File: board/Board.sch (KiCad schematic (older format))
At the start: 57 parts, among them J1 CONN_02X10, J10 CONN_01X03, J11 CONN_01X03, J12 CONN_01X02, J15 GS3, J16 GS3, J17 GS3, J18 GS2, J19 CONN_01X01, J2 CONN_01X03, J3 CONN_01X03, J4 CONN_01X03, J5 CONN_01X03, J6 CONN_01X03, J7 CONN_01X03, J8 CONN_01X03, J9 CONN_01X03, SW1 SW_Push, U1 STM32F410RBTx, U2 LF33ABDT-TR, U3 ICM-20689, U4 SN74LVC1G04, U5 MS5611, Y1 25 MHz

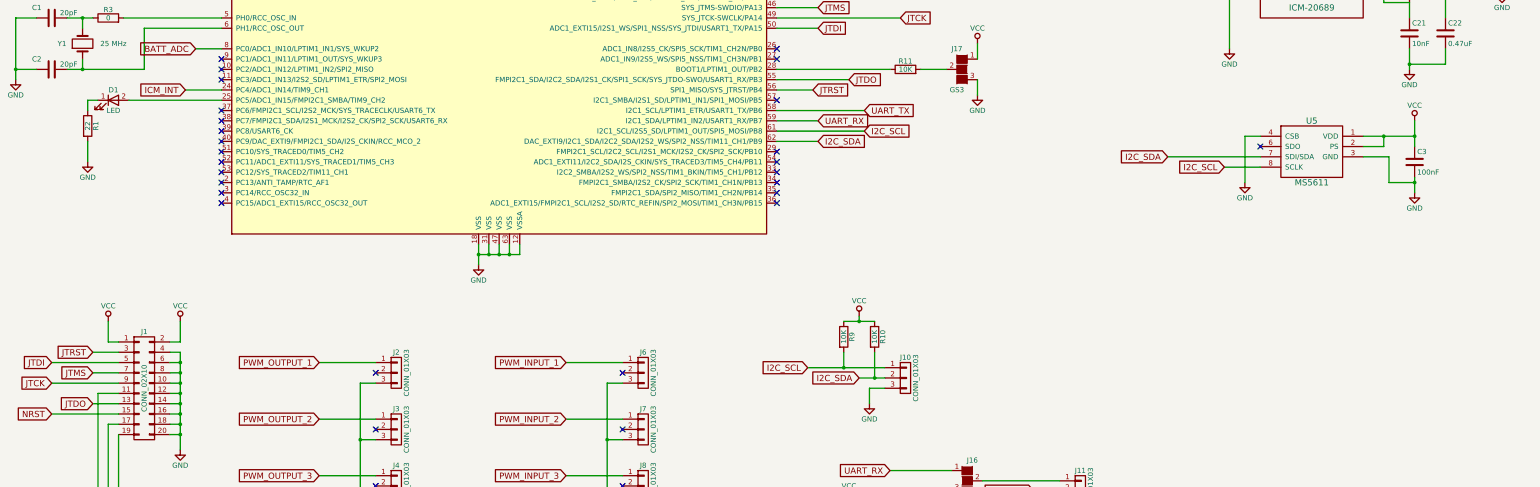
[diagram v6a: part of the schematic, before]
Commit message: added mag 3110 component
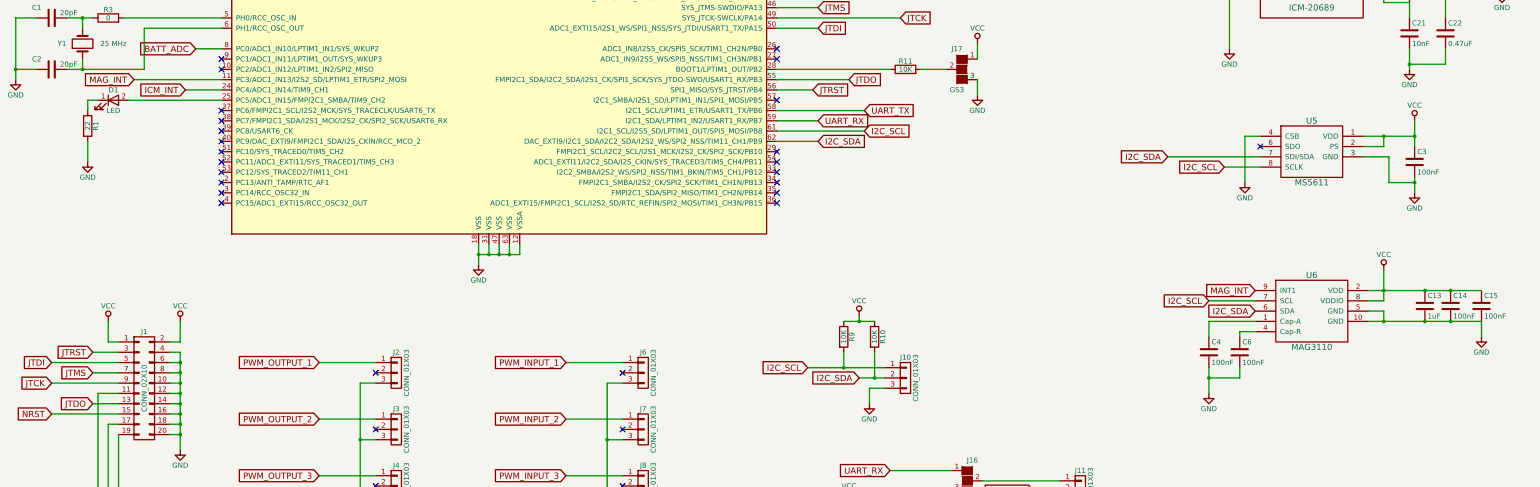
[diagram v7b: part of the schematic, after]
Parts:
- added C13: 1uF, Capacitors_SMD:C_0805_HandSoldering, symbol C
- added C14, C15, C4, C6: 100nF, Capacitors_SMD:C_0805_HandSoldering, symbol C
- added U6: MAG3110, Local_prints:DFN_2x2mm_10pin_0.4pitch, symbol MAG3110
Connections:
- net GND: now also C13.2, C14.2, C15.2, C4.2, C6.2, U6.10 (GND), U6.5 (GND)
- net I2C_SCL: now also U6.7 (SCL)
- net I2C_SDA: now also U6.6 (SDA)
- net VCC: now also C13.1, C14.1, C15.1, U6.2 (VDD), U6.8 (VDDIO)
- net MAG_INT: now reaches U1.11 (PC3/ADC1_IN13/I2S2_SD/LPTIM1_ETR/SPI2_MOSI)
- net MAG_INT: now also U6.9 (INT1)
- new net: C4.1, U6.1 (Cap-A)
- new net: C6.1, U6.4 (Cap-R)
- no-connect marks 32 -> 31

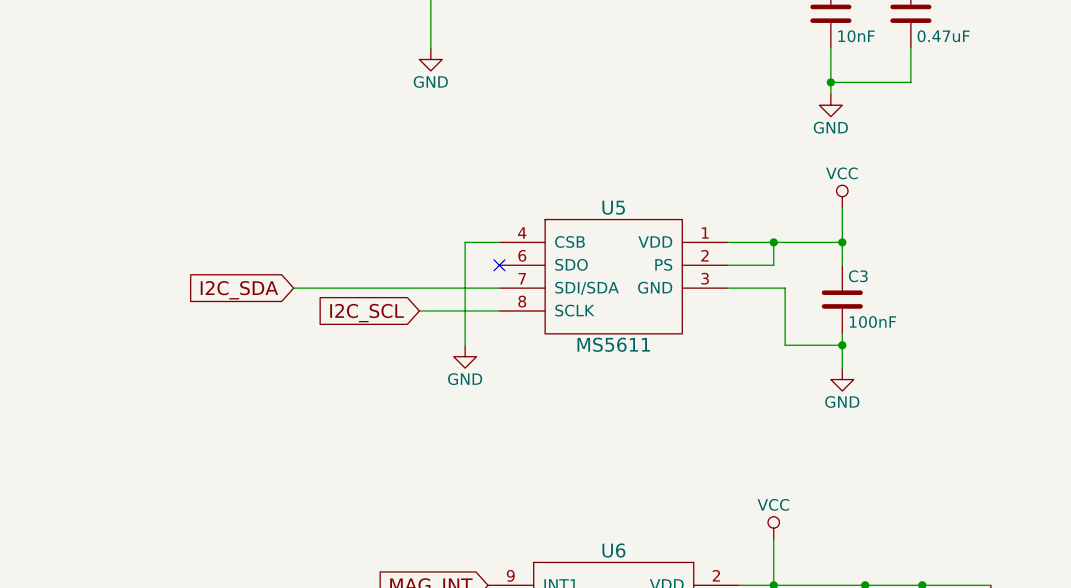
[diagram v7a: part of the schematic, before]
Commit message: replaced barometer
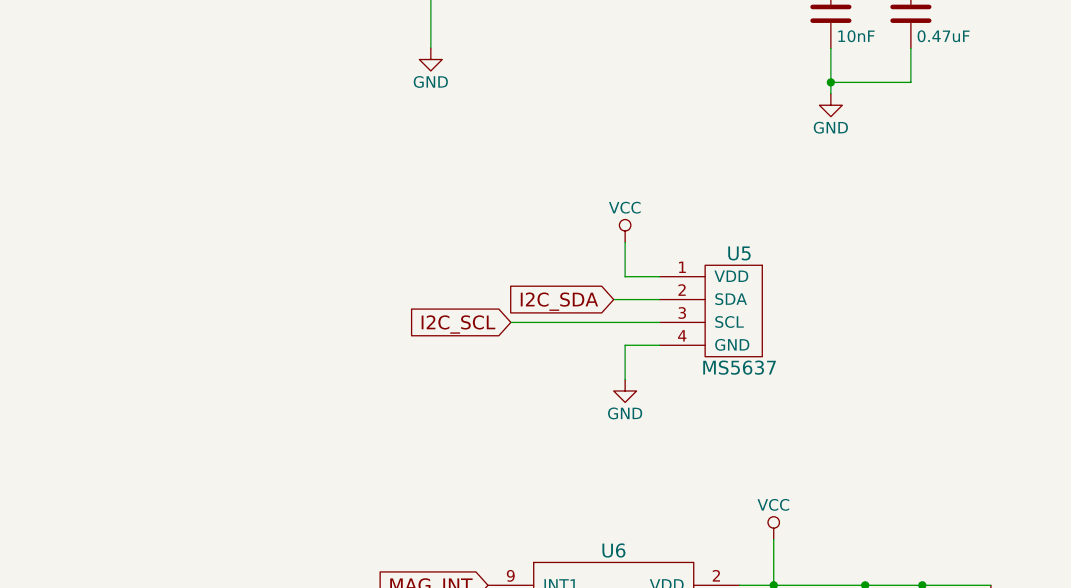
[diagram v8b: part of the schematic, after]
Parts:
- removed C3: 100nF, Capacitors_SMD:C_0805_HandSoldering, symbol C
- removed U5: MS5611, Local_prints:DFN_5x3_8pin, symbol MS5611
- added U5: MS5637, Local_prints:MS5637, symbol MS5637
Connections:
- net GND: now also U5.4 (GND)
- net I2C_SCL: now also U5.3 (SCL)
- net I2C_SDA: now also U5.2 (SDA)
- net VCC: now also U5.1 (VDD)
- no-connect marks 31 -> 30
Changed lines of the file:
@@
 LIBS:ms5611
 LIBS:mag3110
+LIBS:ms5637
+LIBS:Board-cache
 EELAYER 25 0
 EELAYER END
@@
 NoConn ~ 8200 4750
 NoConn ~ 8200 4150
-$Comp
-L MS5611 U5
-U 1 1 58F7F3A8
-P 13400 4650
-F 0 "U5" H 13400 4950 60  0000 C CNN
-F 1 "MS5611" H 13400 4350 60  0000 C CNN
-F 2 "Local_prints:DFN_5x3_8pin" H 13400 4500 60  0001 C CNN
-F 3 "" H 13400 4500 60  0001 C CNN
-	1    13400 4650
-	1    0    0    -1
-$EndComp
-Text GLabel 12550 4800 0    60   Input ~ 0
+Text GLabel 12950 4850 0    60   Input ~ 0
 I2C_SCL
-Text GLabel 12000 4700 0    60   Input ~ 0
+Text GLabel 13400 4750 0    60   Input ~ 0
 I2C_SDA
 $Comp
-L GND #PWR043
-U 1 1 58F85FBB
-P 12750 4950
-F 0 "#PWR043" H 12750 4700 50  0001 C CNN
-F 1 "GND" H 12750 4800 50  0000 C CNN
-F 2 "" H 12750 4950 50  0001 C CNN
-F 3 "" H 12750 4950 50  0001 C CNN
-	1    12750 4950
-	1    0    0    -1
-$EndComp
-NoConn ~ 12900 4600
-$Comp
-L VCC #PWR044
+L VCC #PWR043
 U 1 1 58F863D2
-P 14400 4350
-F 0 "#PWR044" H 14400 4200 50  0001 C CNN
-F 1 "VCC" H 14400 4500 50  0000 C CNN
-F 2 "" H 14400 4350 50  0001 C CNN
-F 3 "" H 14400 4350 50  0001 C CNN
-	1    14400 4350
-	1    0    0    -1
-$EndComp
-$Comp
-L C C3
-U 1 1 58F867FF
-P 14400 4750
-F 0 "C3" H 14425 4850 50  0000 L CNN
-F 1 "100nF" H 14425 4650 50  0000 L CNN
-F 2 "Capacitors_SMD:C_0805_HandSoldering" H 14438 4600 50  0001 C CNN
-F 3 "" H 14400 4750 50  0001 C CNN
-	1    14400 4750
-	1    0    0    -1
-$EndComp
-$Comp
-L GND #PWR045
+P 13450 4500
+F 0 "#PWR043" H 13450 4350 50  0001 C CNN
+F 1 "VCC" H 13450 4650 50  0000 C CNN
+F 2 "" H 13450 4500 50  0001 C CNN
+F 3 "" H 13450 4500 50  0001 C CNN
+	1    13450 4500
+	1    0    0    -1
+$EndComp
+$Comp
+L GND #PWR044
 U 1 1 58F86E8C
-P 14400 5050
-F 0 "#PWR045" H 14400 4800 50  0001 C CNN
-F 1 "GND" H 14400 4900 50  0000 C CNN
-F 2 "" H 14400 5050 50  0001 C CNN
-F 3 "" H 14400 5050 50  0001 C CNN
-	1    14400 5050
+P 13450 5100
+F 0 "#PWR044" H 13450 4850 50  0001 C CNN
+F 1 "GND" H 13450 4950 50  0000 C CNN
+F 2 "" H 13450 5100 50  0001 C CNN
+F 3 "" H 13450 5100 50  0001 C CNN
+	1    13450 5100
 	1    0    0    -1
 $EndComp
@@
 $EndComp
 $Comp
-L GND #PWR046
+L GND #PWR045
 U 1 1 58F9DAF3
 P 12400 7000
-F 0 "#PWR046" H 12400 6750 50  0001 C CNN
+F 0 "#PWR045" H 12400 6750 50  0001 C CNN
 F 1 "GND" H 12400 6850 50  0000 C CNN
 F 2 "" H 12400 7000 50  0001 C CNN
@@
 $EndComp
 $Comp
-L VCC #PWR047
+L VCC #PWR046
 U 1 1 58FA1A71
 P 14100 5800
-F 0 "#PWR047" H 14100 5650 50  0001 C CNN
+F 0 "#PWR046" H 14100 5650 50  0001 C CNN
 F 1 "VCC" H 14100 5950 50  0000 C CNN
 F 2 "" H 14100 5800 50  0001 C CNN
@@
 $EndComp
 $Comp
-L GND #PWR048
+L GND #PWR047
 U 1 1 58FA2856
 P 15050 6450
-F 0 "#PWR048" H 15050 6200 50  0001 C CNN
+F 0 "#PWR047" H 15050 6200 50  0001 C CNN
 F 1 "GND" H 15050 6300 50  0000 C CNN
 F 2 "" H 15050 6450 50  0001 C CNN
@@
 Wire Wire Line
 	9550 7950 9900 7950
-Wire Wire Line
-	12900 4800 12550 4800
-Wire Wire Line
-	12000 4700 12900 4700
-Wire Wire Line
-	12900 4500 12750 4500
-Wire Wire Line
-	12750 4500 12750 4950
-Wire Wire Line
-	13900 4500 14400 4500
-Wire Wire Line
-	14400 4350 14400 4600
-Connection ~ 14400 4500
-Wire Wire Line
-	13900 4600 14100 4600
-Wire Wire Line
-	14100 4600 14100 4500
-Connection ~ 14100 4500
-Wire Wire Line
-	14400 4900 14400 5050
-Wire Wire Line
-	13900 4700 14150 4700
-Wire Wire Line
-	14150 4700 14150 4950
-Wire Wire Line
-	14150 4950 14400 4950
-Connection ~ 14400 4950
 Wire Wire Line
 	2800 3950 1950 3950
@@
 	14100 6200 14100 6300
 Connection ~ 14100 6300
+$Comp
+L MS5637 U5
+U 1 1 58F8A478
+P 13900 4800
+F 0 "U5" H 13950 5050 60  0000 C CNN
+F 1 "MS5637" H 13950 4550 60  0000 C CNN
+F 2 "Local_prints:MS5637" H 13900 4800 60  0001 C CNN
+F 3 "" H 13900 4800 60  0001 C CNN
+	1    13900 4800
+	1    0    0    -1
+$EndComp
+Wire Wire Line
+	13600 4650 13450 4650
+Wire Wire Line
+	13450 4650 13450 4500
+Wire Wire Line
+	13600 4950 13450 4950
+Wire Wire Line
+	13450 4950 13450 5100
+Wire Wire Line
+	13600 4750 13400 4750
+Wire Wire Line
+	12950 4850 13600 4850
 $EndSCHEMATC
